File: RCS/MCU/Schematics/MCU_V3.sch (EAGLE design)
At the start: 19 parts, among them IC1 FT232RL, Q1 8 MHz, U1 ATMEGA328P_TQFP, X1 USB-A

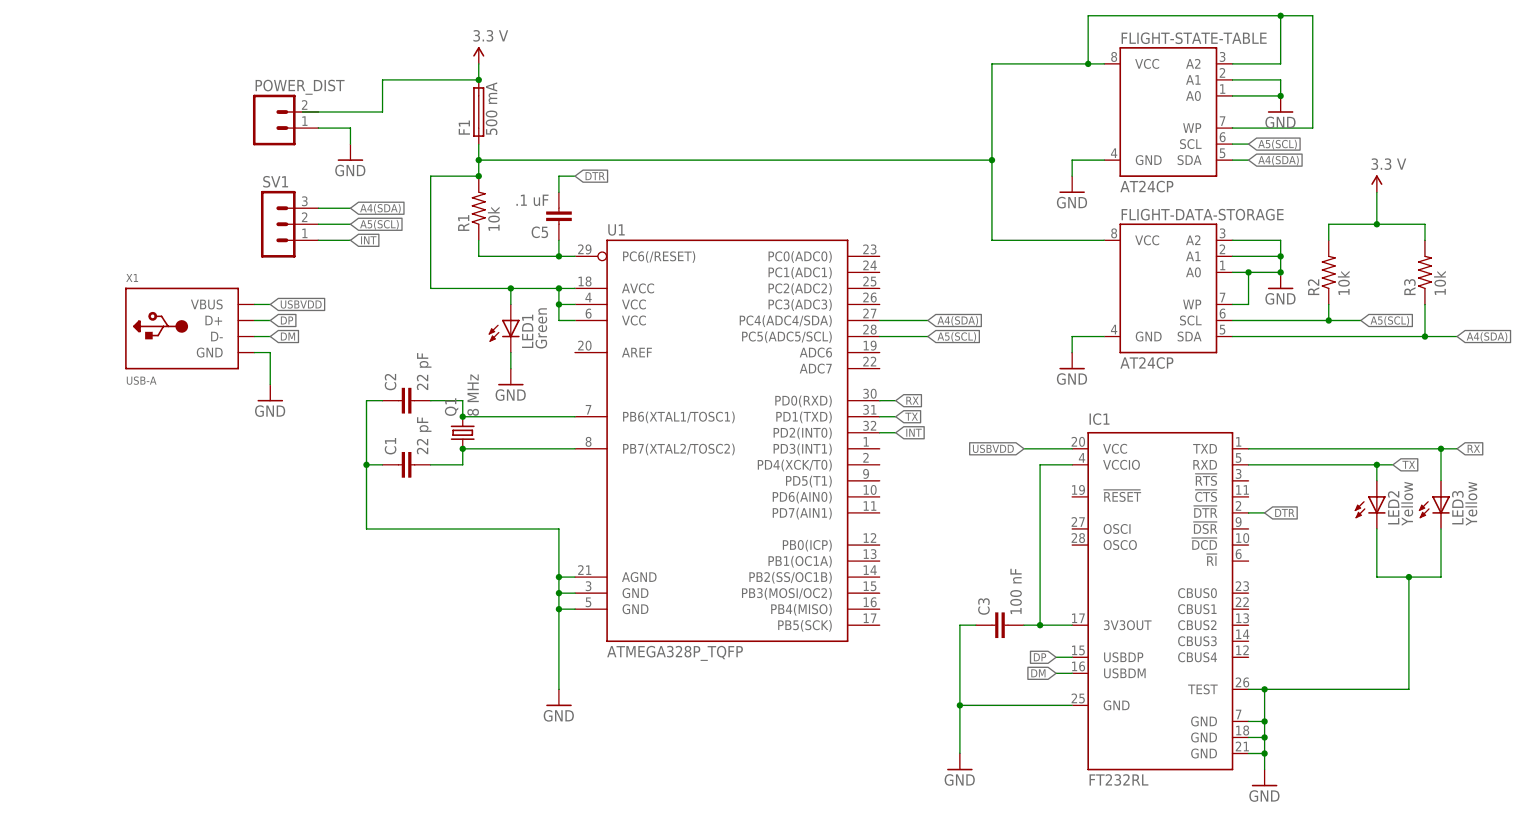
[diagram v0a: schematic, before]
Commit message: Added Resistors in series with LEDs
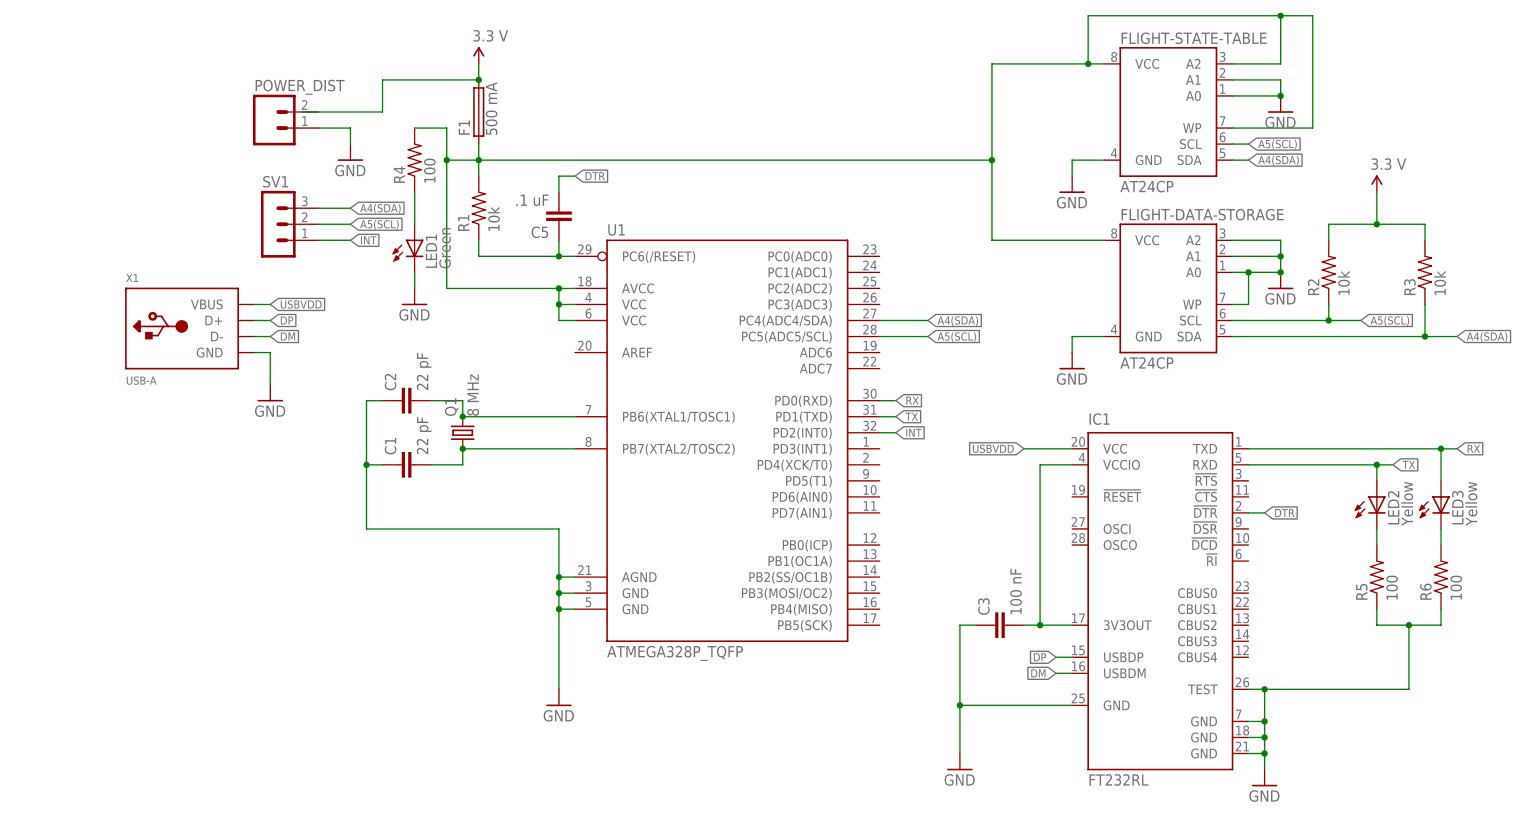
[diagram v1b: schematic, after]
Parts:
- added R4, R5, R6: 100, resistor:R-US_R0805
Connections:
- new net N$10: LED3.C, R6.2
- new net N$6: LED1.A, R4.1
- new net N$9: LED2.C, R5.2
- net GND: now also R5.1, R6.1; no longer LED2.C, LED3.C
- net N$5: now also R4.2; no longer LED1.A
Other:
- moved on the sheet: LED1
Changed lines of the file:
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@@
 <part name="LED2" library="adafruit" deviceset="LED" device="" value="Yellow"/>
 <part name="LED3" library="adafruit" deviceset="LED" device="" value="Yellow"/>
+<part name="R4" library="resistor" deviceset="R-US_" device="R0805" value="100"/>
+<part name="R5" library="resistor" deviceset="R-US_" device="R0805" value="100"/>
+<part name="R6" library="resistor" deviceset="R-US_" device="R0805" value="100"/>
 </parts>
 <sheets>
@@
 <instance part="U1" gate="U$1" x="60.96" y="43.18"/>
 <instance part="SV1" gate="G$1" x="-12.7" y="78.74"/>
-<instance part="LED1" gate="G$1" x="25.4" y="63.5"/>
-<instance part="GND10" gate="1" x="25.4" y="53.34"/>
+<instance part="LED1" gate="G$1" x="10.16" y="76.2"/>
+<instance part="GND10" gate="1" x="10.16" y="66.04"/>
 <instance part="LED2" gate="G$1" x="162.56" y="35.56"/>
 <instance part="LED3" gate="G$1" x="172.72" y="35.56"/>
+<instance part="R4" gate="G$1" x="10.16" y="88.9" rot="R90"/>
+<instance part="R5" gate="G$1" x="162.56" y="22.86" rot="R90"/>
+<instance part="R6" gate="G$1" x="172.72" y="22.86" rot="R90"/>
 </instances>
 <busses>
@@
 <junction x="144.78" y="0"/>
 <wire x1="144.78" y1="5.08" x2="167.64" y2="5.08" width="0.1524" layer="91"/>
-<wire x1="167.64" y1="5.08" x2="167.64" y2="22.86" width="0.1524" layer="91"/>
 <junction x="144.78" y="5.08"/>
-<pinref part="LED2" gate="G$1" pin="C"/>
-<wire x1="162.56" y1="30.48" x2="162.56" y2="22.86" width="0.1524" layer="91"/>
-<pinref part="LED3" gate="G$1" pin="C"/>
-<wire x1="162.56" y1="22.86" x2="167.64" y2="22.86" width="0.1524" layer="91"/>
-<wire x1="167.64" y1="22.86" x2="172.72" y2="22.86" width="0.1524" layer="91"/>
-<wire x1="172.72" y1="22.86" x2="172.72" y2="30.48" width="0.1524" layer="91"/>
-<junction x="167.64" y="22.86"/>
+<pinref part="R5" gate="G$1" pin="1"/>
+<wire x1="162.56" y1="17.78" x2="162.56" y2="15.24" width="0.1524" layer="91"/>
+<pinref part="R6" gate="G$1" pin="1"/>
+<wire x1="162.56" y1="15.24" x2="167.64" y2="15.24" width="0.1524" layer="91"/>
+<wire x1="167.64" y1="15.24" x2="172.72" y2="15.24" width="0.1524" layer="91"/>
+<wire x1="172.72" y1="15.24" x2="172.72" y2="17.78" width="0.1524" layer="91"/>
+<wire x1="167.64" y1="5.08" x2="167.64" y2="15.24" width="0.1524" layer="91"/>
+<junction x="167.64" y="15.24"/>
 </segment>
 <segment>
@@
 <pinref part="GND10" gate="1" pin="GND"/>
 <pinref part="LED1" gate="G$1" pin="C"/>
-<wire x1="25.4" y1="55.88" x2="25.4" y2="58.42" width="0.1524" layer="91"/>
+<wire x1="10.16" y1="68.58" x2="10.16" y2="71.12" width="0.1524" layer="91"/>
 </segment>
 </net>
@@
 <pinref part="R1" gate="G$1" pin="2"/>
 <wire x1="147.32" y1="111.76" x2="116.84" y2="111.76" width="0.1524" layer="91"/>
-<wire x1="35.56" y1="68.58" x2="33.02" y2="68.58" width="0.1524" layer="91"/>
-<wire x1="33.02" y1="68.58" x2="25.4" y2="68.58" width="0.1524" layer="91"/>
-<wire x1="25.4" y1="68.58" x2="12.7" y2="68.58" width="0.1524" layer="91"/>
-<wire x1="12.7" y1="68.58" x2="12.7" y2="86.36" width="0.1524" layer="91"/>
-<wire x1="12.7" y1="86.36" x2="20.32" y2="86.36" width="0.1524" layer="91"/>
-<wire x1="33.02" y1="68.58" x2="33.02" y2="66.04" width="0.1524" layer="91"/>
-<junction x="33.02" y="68.58"/>
-<wire x1="33.02" y1="66.04" x2="35.56" y2="66.04" width="0.1524" layer="91"/>
 <pinref part="F1" gate="1" pin="1"/>
 <wire x1="20.32" y1="86.36" x2="20.32" y2="88.9" width="0.1524" layer="91"/>
-<junction x="20.32" y="86.36"/>
 <wire x1="20.32" y1="88.9" x2="20.32" y2="91.44" width="0.1524" layer="91"/>
 <wire x1="20.32" y1="88.9" x2="101.6" y2="88.9" width="0.1524" layer="91"/>
@@
 <wire x1="116.84" y1="111.76" x2="116.84" y2="104.14" width="0.1524" layer="91"/>
 <junction x="116.84" y="104.14"/>
+<junction x="147.32" y="111.76"/>
+<pinref part="R4" gate="G$1" pin="2"/>
+<wire x1="10.16" y1="93.98" x2="15.24" y2="93.98" width="0.1524" layer="91"/>
+<wire x1="15.24" y1="93.98" x2="15.24" y2="88.9" width="0.1524" layer="91"/>
+<wire x1="15.24" y1="88.9" x2="20.32" y2="88.9" width="0.1524" layer="91"/>
+<wire x1="15.24" y1="88.9" x2="15.24" y2="68.58" width="0.1524" layer="91"/>
+<junction x="15.24" y="88.9"/>
+<pinref part="U1" gate="U$1" pin="VCC@6"/>
 <pinref part="U1" gate="U$1" pin="VCC@4"/>
 <pinref part="U1" gate="U$1" pin="AVCC"/>
+<wire x1="35.56" y1="68.58" x2="33.02" y2="68.58" width="0.1524" layer="91"/>
+<wire x1="33.02" y1="68.58" x2="33.02" y2="66.04" width="0.1524" layer="91"/>
+<wire x1="33.02" y1="66.04" x2="35.56" y2="66.04" width="0.1524" layer="91"/>
+<junction x="33.02" y="66.04"/>
 <wire x1="33.02" y1="66.04" x2="33.02" y2="63.5" width="0.1524" layer="91"/>
-<junction x="33.02" y="66.04"/>
-<pinref part="U1" gate="U$1" pin="VCC@6"/>
 <wire x1="33.02" y1="63.5" x2="35.56" y2="63.5" width="0.1524" layer="91"/>
-<junction x="147.32" y="111.76"/>
-<pinref part="LED1" gate="G$1" pin="A"/>
-<wire x1="25.4" y1="66.04" x2="25.4" y2="68.58" width="0.1524" layer="91"/>
-<junction x="25.4" y="68.58"/>
+<wire x1="15.24" y1="68.58" x2="33.02" y2="68.58" width="0.1524" layer="91"/>
+<junction x="33.02" y="68.58"/>
 </segment>
 </net>
@@
 </segment>
 </net>
+<net name="N$6" class="0">
+<segment>
+<pinref part="LED1" gate="G$1" pin="A"/>
+<pinref part="R4" gate="G$1" pin="1"/>
+<wire x1="10.16" y1="78.74" x2="10.16" y2="83.82" width="0.1524" layer="91"/>
+</segment>
+</net>
+<net name="N$9" class="0">
+<segment>
+<pinref part="LED2" gate="G$1" pin="C"/>
+<pinref part="R5" gate="G$1" pin="2"/>
+<wire x1="162.56" y1="30.48" x2="162.56" y2="27.94" width="0.1524" layer="91"/>
+</segment>
+</net>
+<net name="N$10" class="0">
+<segment>
+<pinref part="LED3" gate="G$1" pin="C"/>
+<pinref part="R6" gate="G$1" pin="2"/>
+<wire x1="172.72" y1="30.48" x2="172.72" y2="27.94" width="0.1524" layer="91"/>
+</segment>
+</net>

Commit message: Added GPIO LED and Capacitors on USB line
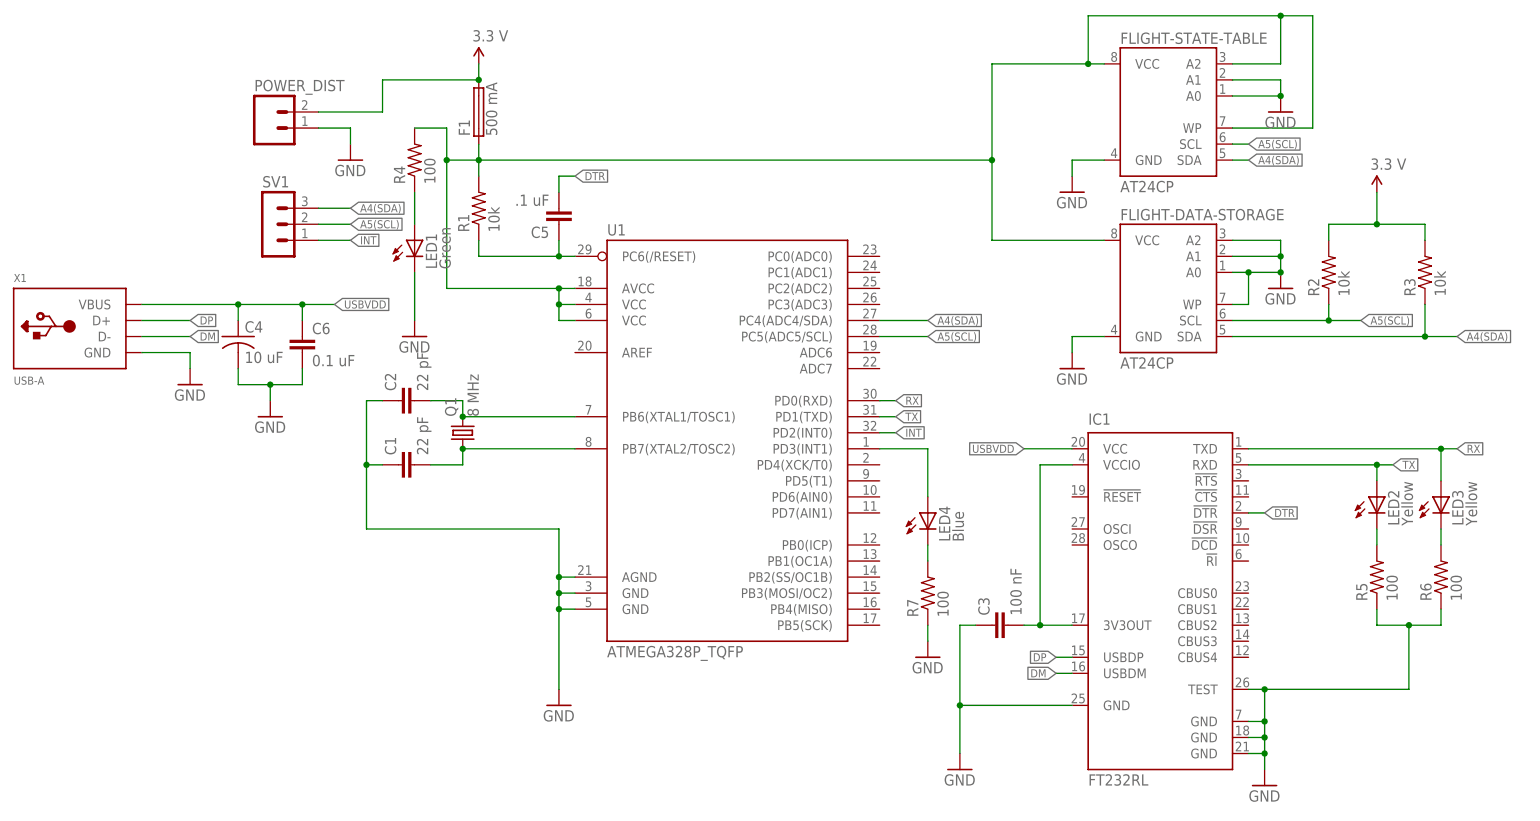
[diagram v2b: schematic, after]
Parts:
- added C4: 10 uF, adafruit:C-US025-024X044
- added C6: 0.1 uF, capacitor-wima:C2,5-3
- added LED4: Blue, adafruit:LED5MM
- added R7: 100, resistor:R-US_R0805
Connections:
- new net N$4: LED4.A, U1.PD3(INT1)
- new net N$8: LED4.C, R7.2
- net GND: now also C4.2, C6.2, R7.1
- net USBVDD: now also C4.1, C6.1
- net VDD: now also POWER_DIST.2
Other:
- moved on the sheet: X1
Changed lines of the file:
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@@
 <part name="R5" library="resistor" deviceset="R-US_" device="R0805" value="100"/>
 <part name="R6" library="resistor" deviceset="R-US_" device="R0805" value="100"/>
+<part name="LED4" library="adafruit" deviceset="LED" device="5MM" value="Blue"/>
+<part name="R7" library="resistor" deviceset="R-US_" device="R0805" value="100"/>
+<part name="GND11" library="supply1" deviceset="GND" device=""/>
+<part name="C4" library="adafruit" deviceset="C-US" device="025-024X044" value="10 uF"/>
+<part name="C6" library="capacitor-wima" deviceset="C" device="2,5-3" value="0.1 uF"/>
+<part name="GND12" library="supply1" deviceset="GND" device=""/>
 </parts>
 <sheets>
@@
 <instance part="C3" gate="G$1" x="101.6" y="15.24" rot="R90"/>
 <instance part="GND5" gate="1" x="96.52" y="-7.62"/>
-<instance part="X1" gate="G$1" x="-25.4" y="60.96"/>
+<instance part="X1" gate="G$1" x="-43.18" y="60.96"/>
 <instance part="GND6" gate="1" x="144.78" y="-10.16"/>
-<instance part="GND7" gate="1" x="-12.7" y="50.8"/>
+<instance part="GND7" gate="1" x="-25.4" y="53.34"/>
 <instance part="C5" gate="G$1" x="33.02" y="78.74" rot="R180"/>
 <instance part="R2" gate="G$1" x="154.94" y="71.12" rot="R90"/>
@@
 <instance part="SV1" gate="G$1" x="-12.7" y="78.74"/>
 <instance part="LED1" gate="G$1" x="10.16" y="76.2"/>
-<instance part="GND10" gate="1" x="10.16" y="66.04"/>
+<instance part="GND10" gate="1" x="10.16" y="60.96"/>
 <instance part="LED2" gate="G$1" x="162.56" y="35.56"/>
 <instance part="LED3" gate="G$1" x="172.72" y="35.56"/>
@@
 <instance part="R5" gate="G$1" x="162.56" y="22.86" rot="R90"/>
 <instance part="R6" gate="G$1" x="172.72" y="22.86" rot="R90"/>
+<instance part="LED4" gate="G$1" x="91.44" y="33.02"/>
+<instance part="R7" gate="G$1" x="91.44" y="20.32" rot="R90"/>
+<instance part="GND11" gate="1" x="91.44" y="10.16"/>
+<instance part="C4" gate="G$1" x="-17.78" y="60.96"/>
+<instance part="C6" gate="G$1" x="-7.62" y="60.96"/>
+<instance part="GND12" gate="1" x="-12.7" y="48.26"/>
 </instances>
 <busses>
@@
 </segment>
 <segment>
-<wire x1="-12.7" y1="58.42" x2="-12.7" y2="53.34" width="0.1524" layer="91"/>
+<wire x1="-25.4" y1="58.42" x2="-25.4" y2="55.88" width="0.1524" layer="91"/>
 <pinref part="X1" gate="G$1" pin="GND"/>
-<wire x1="-12.7" y1="58.42" x2="-15.24" y2="58.42" width="0.1524" layer="91"/>
+<wire x1="-25.4" y1="58.42" x2="-33.02" y2="58.42" width="0.1524" layer="91"/>
 <pinref part="GND7" gate="1" pin="GND"/>
 </segment>
@@
 <pinref part="GND10" gate="1" pin="GND"/>
 <pinref part="LED1" gate="G$1" pin="C"/>
-<wire x1="10.16" y1="68.58" x2="10.16" y2="71.12" width="0.1524" layer="91"/>
+<wire x1="10.16" y1="63.5" x2="10.16" y2="71.12" width="0.1524" layer="91"/>
+</segment>
+<segment>
+<pinref part="R7" gate="G$1" pin="1"/>
+<pinref part="GND11" gate="1" pin="GND"/>
+<wire x1="91.44" y1="15.24" x2="91.44" y2="12.7" width="0.1524" layer="91"/>
+</segment>
+<segment>
+<pinref part="C4" gate="G$1" pin="2"/>
+<wire x1="-17.78" y1="55.88" x2="-17.78" y2="53.34" width="0.1524" layer="91"/>
+<pinref part="GND12" gate="1" pin="GND"/>
+<wire x1="-17.78" y1="53.34" x2="-12.7" y2="53.34" width="0.1524" layer="91"/>
+<wire x1="-12.7" y1="53.34" x2="-12.7" y2="50.8" width="0.1524" layer="91"/>
+<pinref part="C6" gate="G$1" pin="2"/>
+<wire x1="-12.7" y1="53.34" x2="-7.62" y2="53.34" width="0.1524" layer="91"/>
+<wire x1="-7.62" y1="53.34" x2="-7.62" y2="55.88" width="0.1524" layer="91"/>
+<junction x="-12.7" y="53.34"/>
 </segment>
 </net>
@@
 <pinref part="F1" gate="1" pin="2"/>
 <wire x1="20.32" y1="104.14" x2="20.32" y2="101.6" width="0.1524" layer="91"/>
-<wire x1="-7.62" y1="96.52" x2="5.08" y2="96.52" width="0.1524" layer="91"/>
 <wire x1="5.08" y1="96.52" x2="5.08" y2="101.6" width="0.1524" layer="91"/>
 <wire x1="5.08" y1="101.6" x2="20.32" y2="101.6" width="0.1524" layer="91"/>
 <junction x="20.32" y="101.6"/>
+<pinref part="POWER_DIST" gate="G$1" pin="2"/>
+<wire x1="-5.08" y1="96.52" x2="5.08" y2="96.52" width="0.1524" layer="91"/>
 </segment>
 <segment>
@@
 <segment>
 <pinref part="X1" gate="G$1" pin="D-"/>
-<wire x1="-15.24" y1="60.96" x2="-12.7" y2="60.96" width="0.1524" layer="91"/>
-<label x="-12.7" y="60.96" size="1.27" layer="95" xref="yes"/>
+<wire x1="-33.02" y1="60.96" x2="-25.4" y2="60.96" width="0.1524" layer="91"/>
+<label x="-25.4" y="60.96" size="1.27" layer="95" xref="yes"/>
 </segment>
 <segment>
@@
 <segment>
 <pinref part="X1" gate="G$1" pin="D+"/>
-<wire x1="-15.24" y1="63.5" x2="-12.7" y2="63.5" width="0.1524" layer="91"/>
-<label x="-12.7" y="63.5" size="1.27" layer="95" xref="yes"/>
+<wire x1="-33.02" y1="63.5" x2="-25.4" y2="63.5" width="0.1524" layer="91"/>
+<label x="-25.4" y="63.5" size="1.27" layer="95" xref="yes"/>
 </segment>
 <segment>
@@
 <segment>
 <pinref part="X1" gate="G$1" pin="VBUS"/>
-<wire x1="-15.24" y1="66.04" x2="-12.7" y2="66.04" width="0.1524" layer="91"/>
-<label x="-12.7" y="66.04" size="1.27" layer="95" xref="yes"/>
+<wire x1="-33.02" y1="66.04" x2="-17.78" y2="66.04" width="0.1524" layer="91"/>
+<label x="-2.54" y="66.04" size="1.27" layer="95" xref="yes"/>
+<pinref part="C4" gate="G$1" pin="1"/>
+<wire x1="-17.78" y1="66.04" x2="-7.62" y2="66.04" width="0.1524" layer="91"/>
+<wire x1="-7.62" y1="66.04" x2="-2.54" y2="66.04" width="0.1524" layer="91"/>
+<wire x1="-17.78" y1="63.5" x2="-17.78" y2="66.04" width="0.1524" layer="91"/>
+<junction x="-17.78" y="66.04"/>
+<pinref part="C6" gate="G$1" pin="1"/>
+<wire x1="-7.62" y1="63.5" x2="-7.62" y2="66.04" width="0.1524" layer="91"/>
+<junction x="-7.62" y="66.04"/>
 </segment>
 <segment>
@@
 </segment>
 </net>
+<net name="N$4" class="0">
+<segment>
+<pinref part="U1" gate="U$1" pin="PD3(INT1)"/>
+<pinref part="LED4" gate="G$1" pin="A"/>
+<wire x1="83.82" y1="43.18" x2="91.44" y2="43.18" width="0.1524" layer="91"/>
+<wire x1="91.44" y1="43.18" x2="91.44" y2="35.56" width="0.1524" layer="91"/>
+</segment>
+</net>
+<net name="N$8" class="0">
+<segment>
+<pinref part="LED4" gate="G$1" pin="C"/>
+<pinref part="R7" gate="G$1" pin="2"/>
+<wire x1="91.44" y1="27.94" x2="91.44" y2="25.4" width="0.1524" layer="91"/>
+</segment>
+</net>
